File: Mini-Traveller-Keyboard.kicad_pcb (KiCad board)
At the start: 2 copper layers, 243.1 x 76.2 mm, 126 parts, among them P1 USB_C_Receptacle_USB2.0, SW1 SW_Push, U1 ATmega32U4-AU, Y1 16MHz

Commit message: Finished the basic layout and have all the bottom rows ready to go
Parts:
- removed the REF** at (216.2, 142.2)
- removed the REF** at (35.1, 142.2)
- removed the REF** at (140.0, 142.2)
- removed the REF** at (190.0, 142.2)
- removed the REF** at (159.0, 142.2)
- removed the REF** at (118.5, 142.2)
- removed the REF** at (85.1, 142.2)
- removed the REF** at (58.9, 142.2)
- removed the REF** at (32.8, 142.2)
- removed the REF** at (218.5, 142.2)
- removed the REF** at (61.4, 142.2)
- added MX12: MX-NoLED, MX_Only:MXOnly-1U-NoLED, B.Cu at (38.1, -9.51)
- added MX12: MX-NoLED, MX_Only:MXOnly-1U-NoLED, B.Cu at (40.5, -9.51)
- added MX16: MX-NoLED, MX_Only:MXOnly-1U-NoLED, F.Cu at (64.3, -9.53)
- added MX24: MX-NoLED, MX_Only:MXOnly-1U-NoLED, B.Cu at (97.7, -9.53)
- added MX32: MX-NoLED, MX_Only:MXOnly-1U-NoLED, F.Cu at (138.2, -9.53)
- added MX36: MX-NoLED, MX_Only:MXOnly-1U-NoLED, F.Cu at (169.2, -9.54)
- added MX4: MX-NoLED, MX_Only:MXOnly-1U-NoLED, F.Cu at (11.9, -9.54)
- added MX4: MX-NoLED, MX_Only:MXOnly-1U-NoLED, F.Cu at (14.3, -9.53)
- added MX44: MX-NoLED, MX_Only:MXOnly-1U-NoLED, F.Cu at (195.4, -9.53)
- added MX44: MX-NoLED, MX_Only:MXOnly-1U-NoLED, F.Cu at (197.7, -9.51)
- added REF**: 7U, MX_Only:MXOnly-7U-ReversedStabilizers-NoLED, F.Cu at (119.1, -9.54)
- added REF**: 2U, MX_Only:MXOnly-2U-ReversedStabilizers-NoLED, F.Cu at (138.2, -9.53)
- added REF**: 2.25U, MX_Only:MXOnly-2.25U-ReversedStabilizers-NoLED, B.Cu at (97.7, -9.51)
- MX12: moved to B.Cu
- MX28: value 2U -> MX-NoLED; footprint MX_Only:MXOnly-2U-NoLED -> MX_Only:MXOnly-1U-NoLED
- moved C6 198.8 mm to (226.9, -74.5), turned to 180 degrees
- moved U1 176.8 mm to (215.9, -39.2), turned to 225 degrees
- moved R6 171.9 mm to (213.5, -20.8)
- moved C3 171.5 mm to (239.7, -29.7), turned to 0 degrees
- moved C2 164.2 mm to (239.6, -26.4), turned to 180 degrees
- moved D46 159.6 mm to (205.9, -42.9)
- moved D47 159.3 mm to (214.8, -26.2)
- moved R3 159.0 mm to (214.9, -63.0), turned to 180 degrees
- moved R4 156.6 mm to (212.8, -60.6), turned to 180 degrees
- moved D48 156.3 mm to (217.9, -4.83)
- moved D24 156.1 mm to (106.4, -3.20), turned to 90 degrees
- moved D42 156.1 mm to (192.7, -42.9)
- moved D27 155.6 mm to (132.0, -26.3)
- moved D19 155.6 mm to (94.0, -26.3)
- moved D15 155.6 mm to (74.9, -26.3)
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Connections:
- MX28 pad 1: (no net) -> Col6
- MX28 pad 2: (no net) -> Net-(D28-Pad2)
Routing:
- net Row3: track 0.00 -> 157.7 mm
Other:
- board size 243.1 x 76.2 mm -> 243 x 76.2 mm

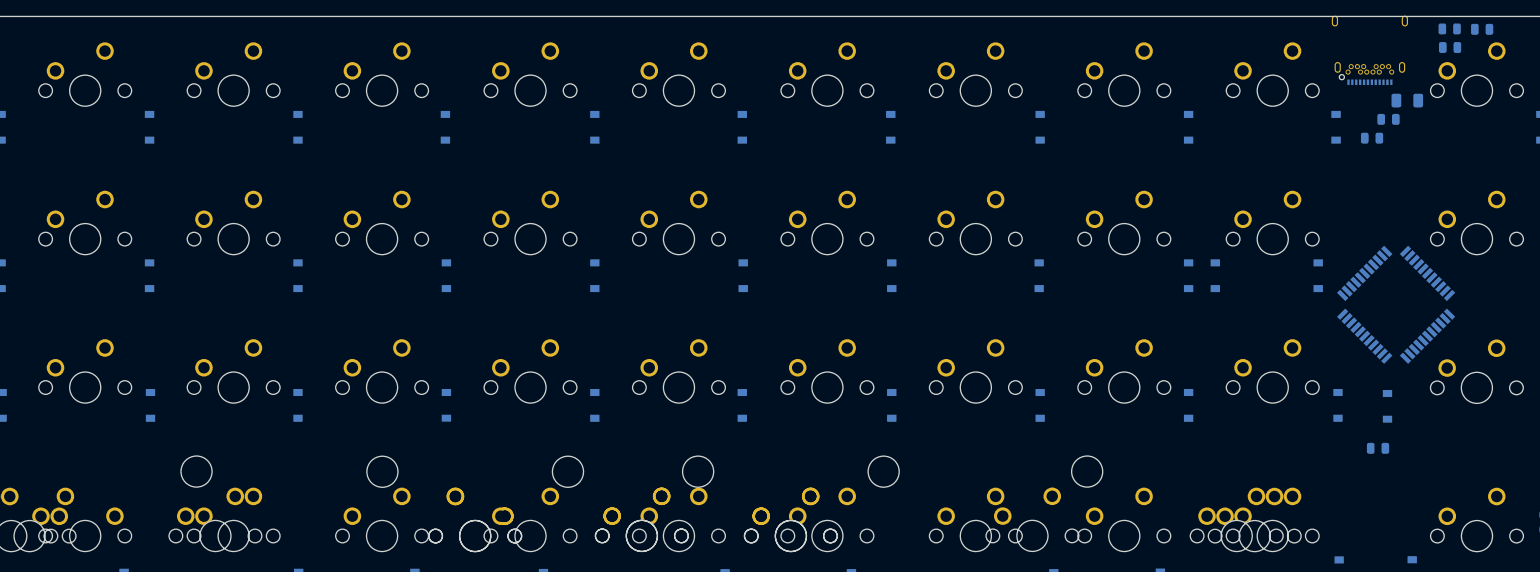
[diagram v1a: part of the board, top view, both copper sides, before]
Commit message: Finished the main layout, cutouts need to be done
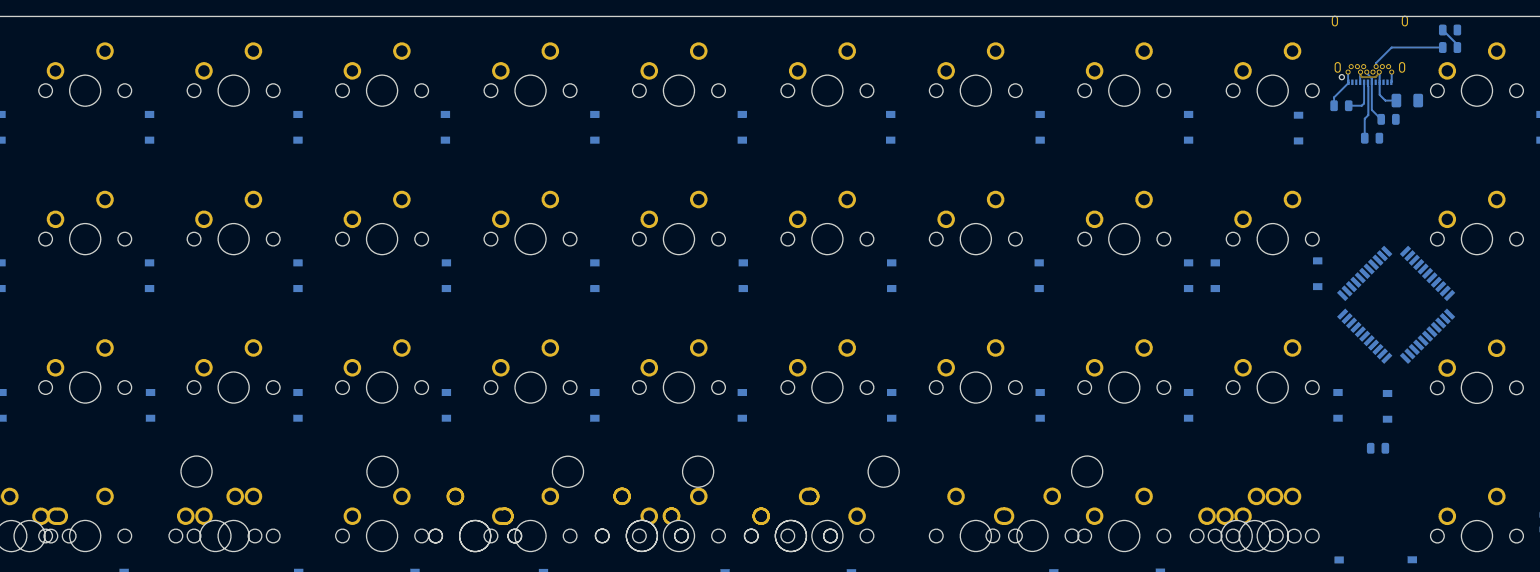
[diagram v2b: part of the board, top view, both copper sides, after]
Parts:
- MX12: moved to F.Cu
- MX28, MX32, MX36, REF**: moved to B.Cu
- moved R1 17.0 mm to (208.8, -64.7), turned to 0 degrees
- moved D41 4.81 mm to (203.3, -61.9)
- moved C6 4.12 mm to (222.8, -74.5)
- moved D46 0.26 mm to (205.8, -43.2)
- turned MX12 to 0 degrees
- turned MX28 to 180 degrees
- turned MX32 to 180 degrees
- turned MX36 to 180 degrees
- turned REF** to 180 degrees
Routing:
- net Net-(F1-Pad2): track 0.00 -> 10.0 mm
- net Net-(P1-PadB5): track 0.00 -> 9.83 mm
- net GND: track 0.00 -> 9.46 mm
- net D+: track 0.00 -> 7.38 mm
- net D-: track 0.00 -> 6.84 mm
- net Net-(P1-PadA5): track 0.00 -> 4.81 mm

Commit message: Main wiring has commenced
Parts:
- moved R6 17.7 mm to (206.1, -36.9), turned to 315 degrees
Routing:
- net Row2: track 0.00 -> 197.6 mm
- net Col7: track 0.00 -> 71.4 mm
- net Col0: track 0.00 -> 61.9 mm
- net Col10: track 0.00 -> 61.8 mm
- net Col3: track 0.00 -> 60.7 mm
- net Col8: track 0.00 -> 60.5 mm
- net Col6: track 0.00 -> 60.0 mm
- net Col2: track 0.00 -> 59.5 mm
- net Col9: track 0.00 -> 59.3 mm
- net Col5: track 0.00 -> 57.7 mm
- net Col11: track 0.00 -> 57.2 mm
- net Col4: track 0.00 -> 57.2 mm
- net Col1: track 0.00 -> 57.2 mm
- net Row3: track 157.7 -> 201.7 mm
- net Row1: track 0.00 -> 35.9 mm
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
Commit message: Finished main PCB design, waiting on silk
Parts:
- added REF**: TestPoint_THTPad_D4.0mm_Drill2.0mm, TestPoint:TestPoint_THTPad_D4.0mm_Drill2.0mm, F.Cu at (210.0, -61.3)
- added REF**: TestPoint_THTPad_D4.0mm_Drill2.0mm, TestPoint:TestPoint_THTPad_D4.0mm_Drill2.0mm, F.Cu at (139.0, -37.3)
- added REF**: TestPoint_THTPad_D4.0mm_Drill2.0mm, TestPoint:TestPoint_THTPad_D4.0mm_Drill2.0mm, F.Cu at (108.3, -56.4)
- added REF**: TestPoint_THTPad_D4.0mm_Drill2.0mm, TestPoint:TestPoint_THTPad_D4.0mm_Drill2.0mm, F.Cu at (32.2, -56.4)
- added REF**: TestPoint_THTPad_D4.0mm_Drill2.0mm, TestPoint:TestPoint_THTPad_D4.0mm_Drill2.0mm, F.Cu at (30.6, -23.1)
- moved SW1 4.57 mm to (5.03, -19.1)
- moved R4 3.25 mm to (214.4, -57.7)
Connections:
- U1 pad 11: Net-(U1-Pad11) -> Col11
- U1 pad 25: Net-(U1-Pad25) -> Col0
- U1 pad 26: Net-(U1-Pad26) -> Col1
- U1 pad 27: Net-(U1-Pad27) -> Col2
- U1 pad 28: Net-(U1-Pad28) -> Col3
- U1 pad 29: Net-(U1-Pad29) -> Col4
- U1 pad 30: Net-(U1-Pad30) -> Col5
- U1 pad 36: Net-(U1-Pad36) -> Col10
- U1 pad 38: Net-(U1-Pad38) -> Col9
- U1 pad 39: Net-(U1-Pad39) -> Col8
- U1 pad 40: Net-(U1-Pad40) -> Col7
- U1 pad 41: Net-(U1-Pad41) -> Col6
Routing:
- net GND: track 15.9 -> 364.0 mm, vias 0 -> 4
- net Net-(R5-Pad2): track 0.00 -> 268.2 mm, vias 0 -> 2
- net Col0: track 61.9 -> 319.4 mm, vias 0 -> 1
- net Col1: track 57.2 -> 277.8 mm, vias 0 -> 1
- net Row0: track 0.00 -> 218.6 mm, vias 0 -> 2
- net Col2: track 59.5 -> 261.5 mm, vias 0 -> 1
- net Col3: track 60.7 -> 254.8 mm, vias 0 -> 1
- net Col4: track 57.2 -> 219.4 mm, vias 0 -> 1
- net Row1: track 35.9 -> 188.1 mm
- net Col5: track 57.7 -> 200.6 mm, vias 0 -> 1
- net +5V: track 0.00 -> 126.9 mm, vias 0 -> 11
- net Col6: track 60.0 -> 186.3 mm, vias 0 -> 1
- net Col7: track 71.4 -> 180.7 mm, vias 0 -> 1
- net Col8: track 60.5 -> 147.3 mm, vias 0 -> 1
- net Col9: track 59.3 -> 120.5 mm, vias 0 -> 1
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- added copper zone on B.Cu, net GND
- added copper zone on F.Cu, net GND
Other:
- board text added: "1275 GT: A Drop-in Ortho Minivan Replacement. Inspired by the iconic classic Mini Clubman model."
- board text added: "By Austin "TuckTuckFloof" Ashmore"

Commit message: files
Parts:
- added D49: WS2812B, LED_SMD:LED_WS2812B_PLCC4_5.0x5.0mm_P3.2mm, F.Cu at (19.1, -69.8)
- added D50: WS2812B, LED_SMD:LED_WS2812B_PLCC4_5.0x5.0mm_P3.2mm, F.Cu at (38.1, -69.8)
- added D51: WS2812B, LED_SMD:LED_WS2812B_PLCC4_5.0x5.0mm_P3.2mm, F.Cu at (57.1, -69.8)
- moved D37 14.2 mm to (175.0, -61.9)
- moved D41 11.1 mm to (192.2, -61.9)
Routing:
- net +5V: track 126.9 -> 308.8 mm, vias 11 -> 13
- net GND: track 364.0 -> 469.0 mm, vias 4 -> 5
- net Net-(D50-Pad2): track 0.00 -> 24.8 mm
- net Net-(D49-Pad2): track 0.00 -> 19.9 mm
- net D+: track 10.5 -> 25.5 mm, vias 0 -> 1
- net Net-(D37-Pad2): track 12.1 -> 26.4 mm
- net Net-(D41-Pad2): track 8.55 -> 19.7 mm
